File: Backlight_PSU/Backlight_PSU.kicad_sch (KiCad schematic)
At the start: 15 parts, among them J1 Conn_01x01, J2 Conn_01x01, J3 Conn_01x01, J4 Conn_01x01, U1 NCP1117-ADJ_SOT223

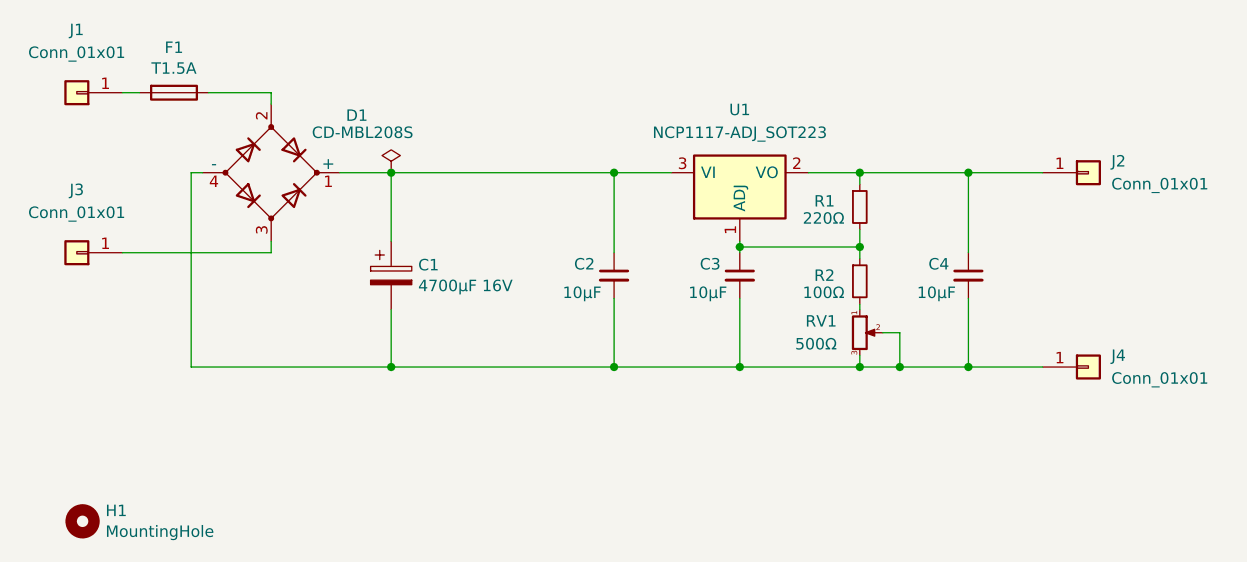
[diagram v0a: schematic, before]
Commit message: Changed capacitor footprint
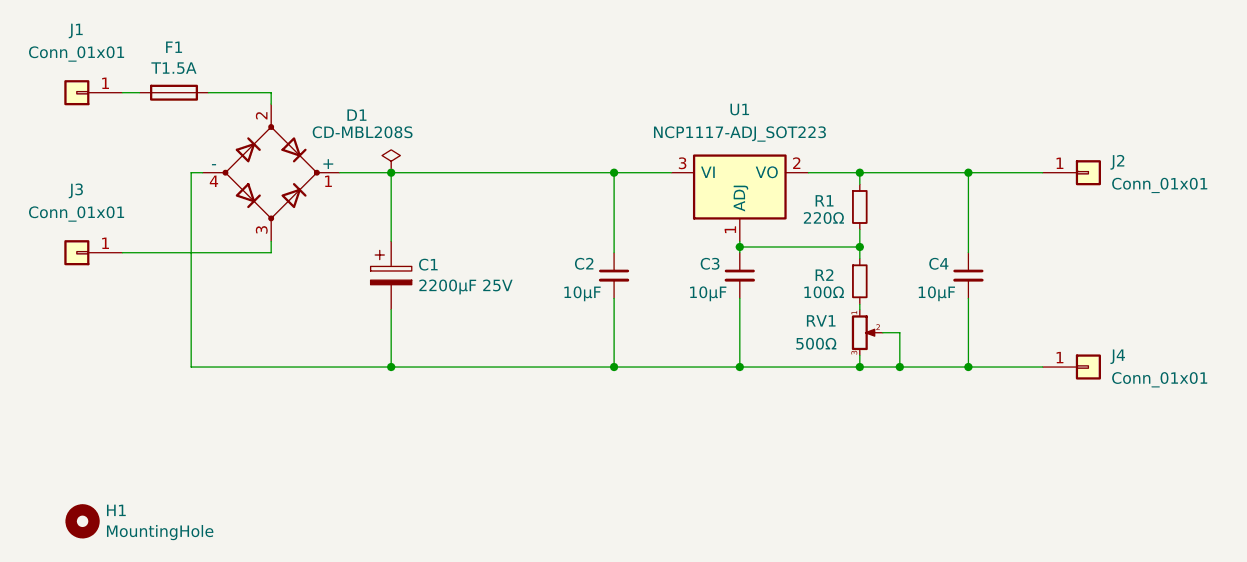
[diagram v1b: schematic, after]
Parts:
- C1: value 4700µF 16V -> 2200µF 25V; footprint Capacitor_SMD:CP_Elec_18x17.5 -> Capacitor_SMD:CP_Elec_16x17.5
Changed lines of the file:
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@@
       (effects (font (size 1.27 1.27)) (justify left))
     )
-    (property "Value" "4700µF 16V" (at 110.9472 93.218 0)
+    (property "Value" "2200µF 25V" (at 110.9472 93.218 0)
       (effects (font (size 1.27 1.27)) (justify left))
     )
-    (property "Footprint" "Capacitor_SMD:CP_Elec_18x17.5" (at 108.9152 95.885 0)
+    (property "Footprint" "Capacitor_SMD:CP_Elec_16x17.5" (at 108.9152 95.885 0)
       (effects (font (size 1.27 1.27)) hide)
     )
@@
       (effects (font (size 1.27 1.27)) hide)
     )
+    (property "Comments" "" (at 107.95 92.075 0)
+      (effects (font (size 1.27 1.27)))
+    )
     (pin "1")

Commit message: Changed fill zone
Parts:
- RV1: footprint Potentiometer_SMD:Potentiometer_TT_35W -> Potentiometer_SMD:Potentiometer_Bourns_TC33X_Vertical
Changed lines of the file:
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@@
       (effects (font (size 1.27 1.27)) (justify right))
     )
-    (property "Footprint" "Potentiometer_SMD:Potentiometer_TT_35W" (at 160.02 98.425 0)
+    (property "Footprint" "Potentiometer_SMD:Potentiometer_Bourns_TC33X_Vertical" (at 160.02 98.425 0)
       (effects (font (size 1.27 1.27)) hide)
     )
@@
       (effects (font (size 1.27 1.27)) hide)
     )
+    (property "Comments" "" (at 160.02 98.425 0)
+      (effects (font (size 1.27 1.27)))
+    )
     (pin "1")

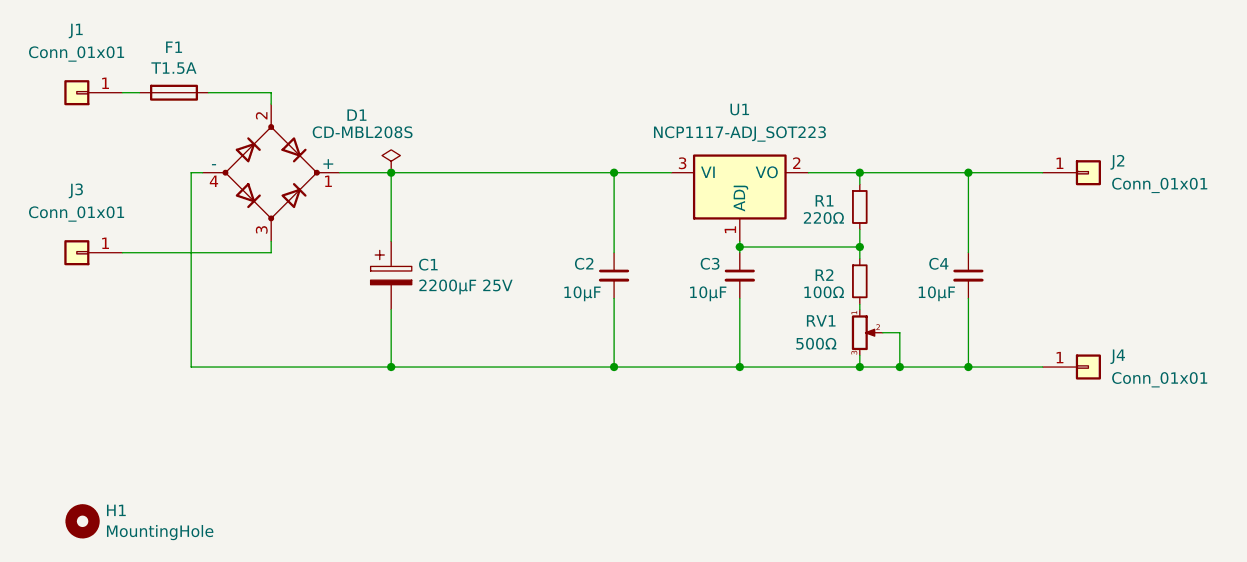
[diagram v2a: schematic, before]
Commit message: Changed component values
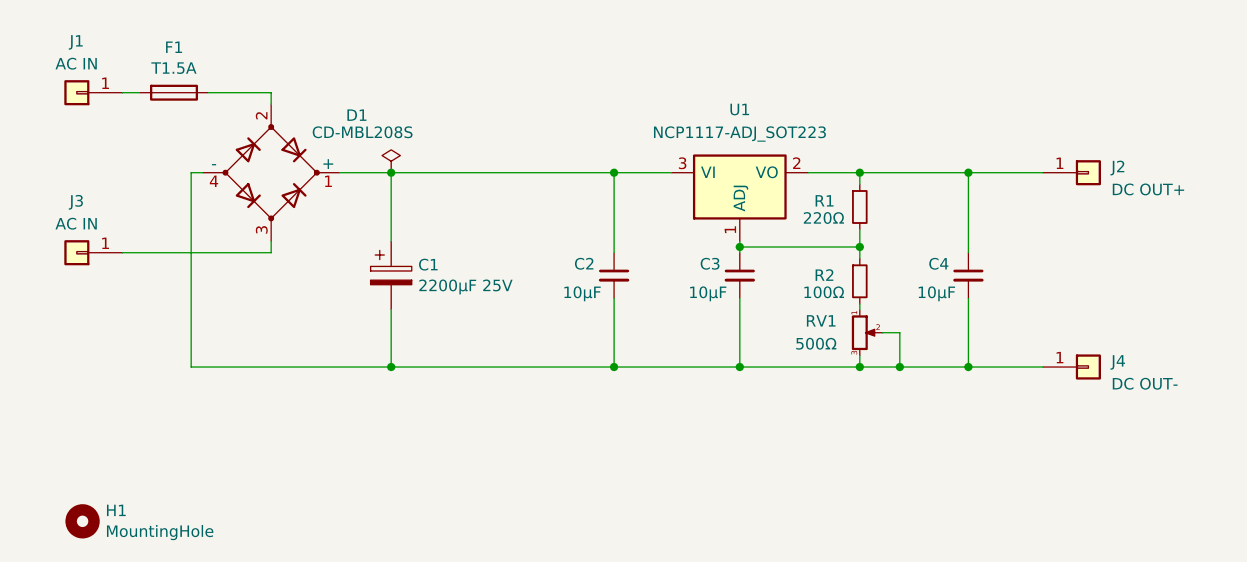
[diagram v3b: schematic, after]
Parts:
- J1, J3: value Conn_01x01 -> AC IN
- J2: value Conn_01x01 -> DC OUT+
- J4: value Conn_01x01 -> DC OUT-
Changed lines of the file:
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@@
   (symbol (lib_id "Connector_Generic:Conn_01x01") (at 185.42 102.235 0) (unit 1)
     (in_bom yes) (on_board yes) (dnp no) (fields_autoplaced)
-    (property "Reference" "J4" (at 187.96 100.9649 0)
+    (property "Reference" "J4" (at 187.96 101.6 0)
       (effects (font (size 1.27 1.27)) (justify left))
     )
-    (property "Value" "Conn_01x01" (at 187.96 103.5049 0)
+    (property "Value" "DC OUT-" (at 187.96 104.14 0)
       (effects (font (size 1.27 1.27)) (justify left))
     )
@@
   (symbol (lib_id "Connector_Generic:Conn_01x01") (at 73.025 89.535 180) (unit 1)
     (in_bom yes) (on_board yes) (dnp no) (fields_autoplaced)
-    (property "Reference" "J3" (at 73.025 82.55 0)
+    (property "Reference" "J3" (at 73.025 83.82 0)
       (effects (font (size 1.27 1.27)))
     )
-    (property "Value" "Conn_01x01" (at 73.025 85.09 0)
+    (property "Value" "AC IN" (at 73.025 86.36 0)
       (effects (font (size 1.27 1.27)))
     )
@@
   (symbol (lib_id "Connector_Generic:Conn_01x01") (at 185.42 80.645 0) (unit 1)
     (in_bom yes) (on_board yes) (dnp no) (fields_autoplaced)
-    (property "Reference" "J2" (at 187.96 79.3749 0)
+    (property "Reference" "J2" (at 187.96 80.01 0)
       (effects (font (size 1.27 1.27)) (justify left))
     )
-    (property "Value" "Conn_01x01" (at 187.96 81.9149 0)
+    (property "Value" "DC OUT+" (at 187.96 82.55 0)
       (effects (font (size 1.27 1.27)) (justify left))
     )
@@
   (symbol (lib_id "Connector_Generic:Conn_01x01") (at 73.025 71.755 180) (unit 1)
     (in_bom yes) (on_board yes) (dnp no) (fields_autoplaced)
-    (property "Reference" "J1" (at 73.025 64.77 0)
+    (property "Reference" "J1" (at 73.025 66.04 0)
       (effects (font (size 1.27 1.27)))
     )
-    (property "Value" "Conn_01x01" (at 73.025 67.31 0)
+    (property "Value" "AC IN" (at 73.025 68.58 0)
       (effects (font (size 1.27 1.27)))
     )

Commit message: Updated component values
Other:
- company: (none) -> Retronics - Bjørner Sandom
- title: (none) -> H11 Backlight PSU
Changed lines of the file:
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@@
 (kicad_sch (version 20230121) (generator eeschema)
   (paper "A4")
+  (title_block
+    (title "H11 Backlight PSU")
+    (company "Retronics - Bjørner Sandom")
+  )
   (junction (at 172.085 80.645) (diameter 0) (color 0 0 0 0)
   )
